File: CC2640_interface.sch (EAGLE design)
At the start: 32 parts, among them Q1 FA-128, Q2 FC-12M

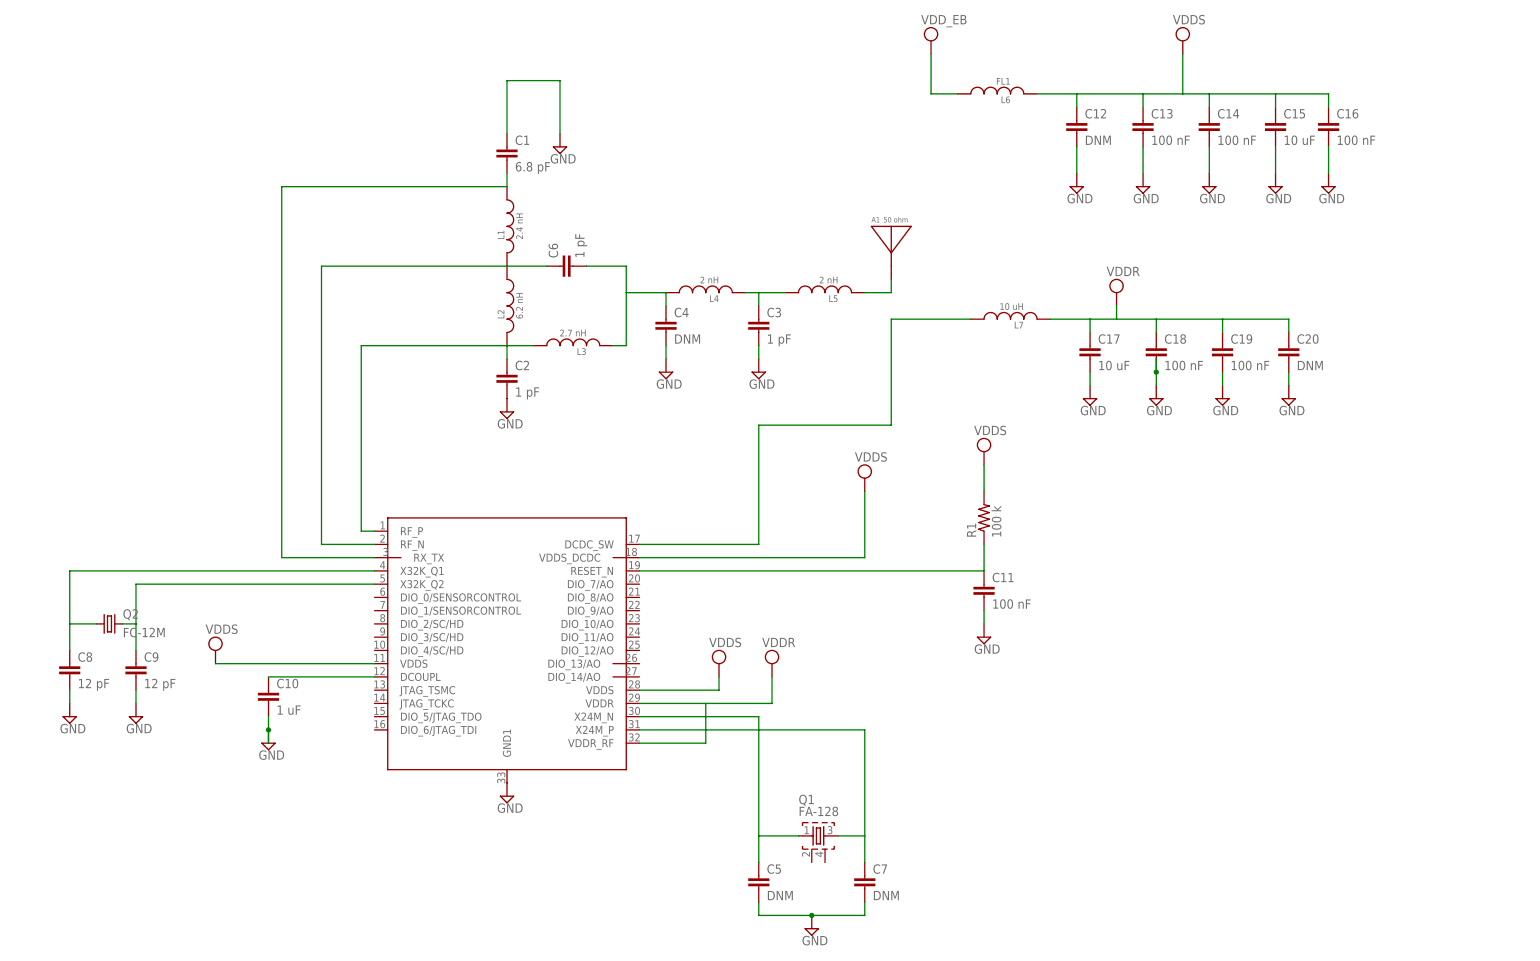
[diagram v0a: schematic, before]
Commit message: cleaned up the schematic
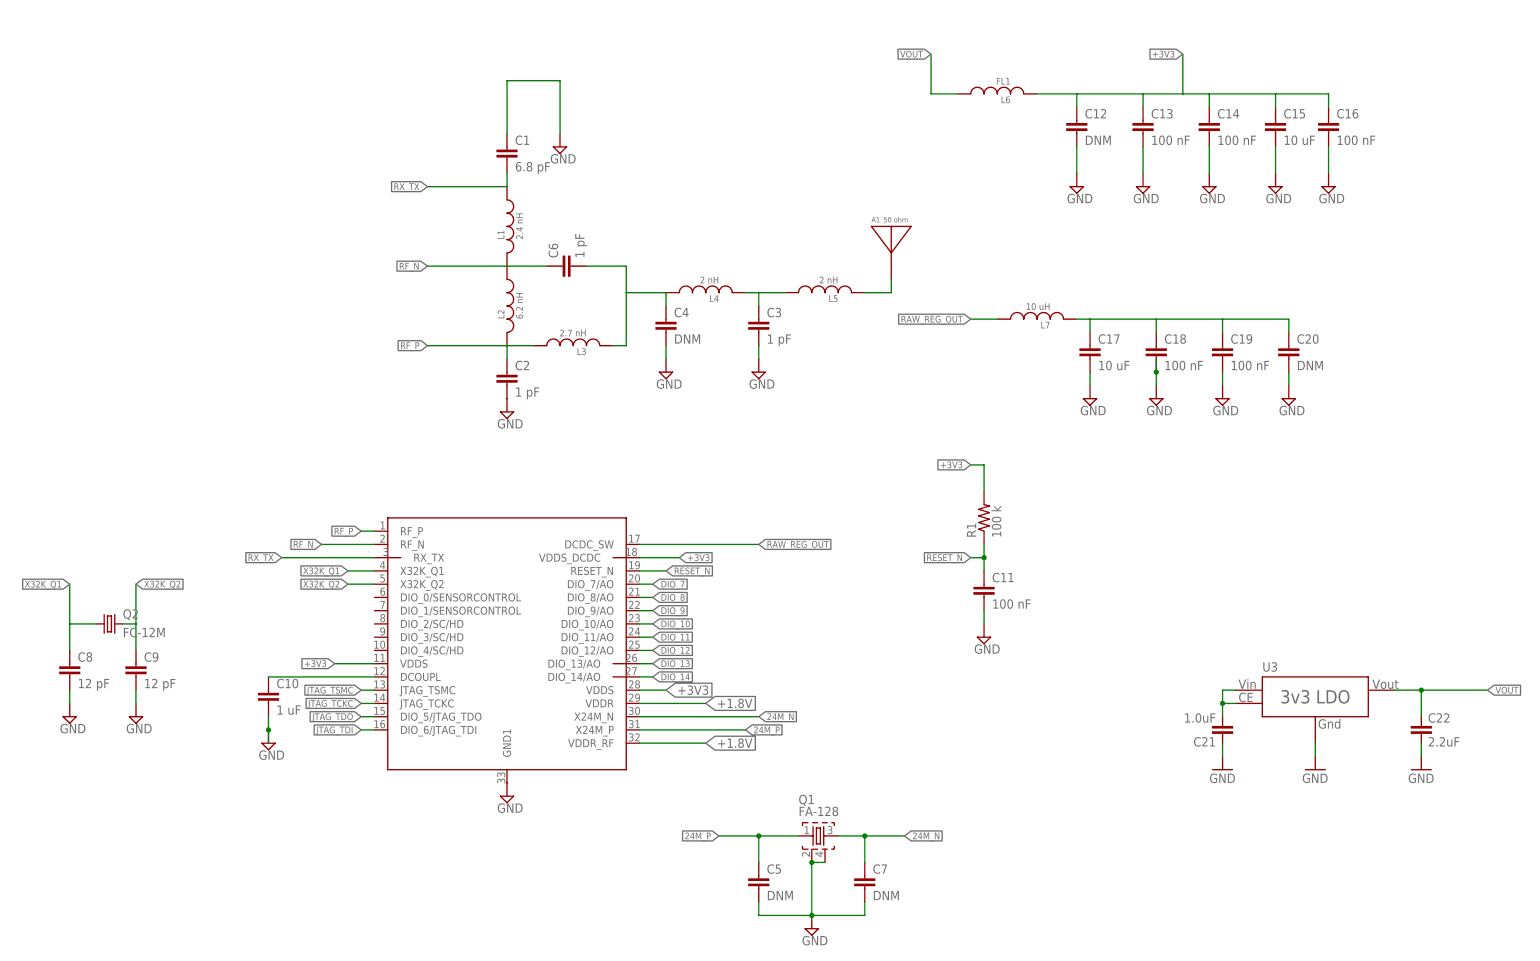
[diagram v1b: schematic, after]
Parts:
- added C21: 1.0uF, Jon_LIB:C-EUC0805
- added C22: 2.2uF, Jon_LIB:C-EUC0805
- added U3: XC6210, MAAV:XC6210
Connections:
- net N$1 renamed RX_TX
- net N$11 renamed DCOUPLE_ME
- net N$14 renamed RAW_REG_OUT
- net N$2 renamed RF_N
- net N$3 renamed RF_P
- net N$6 renamed X32K_Q1
- net N$8 renamed X32K_Q2
- net NRESET renamed RESET_N
- removed net N$10: C7.1, Q1.3, U$1.X24M_P
- removed net N$9: C5.1, Q1.1, U$1.X24M_N
- removed net VDD: C12.1, C13.1, C14.1, C15.1, C16.1, C17.1, C18.1, C19.1, C20.1, L6.1, L6.2, L7.2, R1.2, U$1.VDDR, U$1.VDDR_RF, U$1.VDDS, U$1.VDDS@2, U$1.VDDS_DCDC
- new net +1.8V: C17.1, C18.1, C19.1, C20.1, L7.2, U$1.VDDR, U$1.VDDR_RF
- new net +3V3: C12.1, C13.1, C14.1, C15.1, C16.1, L6.2, R1.2, U$1.VDDS, U$1.VDDS@2, U$1.VDDS_DCDC
- new net 24M_N: C7.1, Q1.3, U$1.X24M_N
- new net 24M_P: C5.1, Q1.1, U$1.X24M_P
- new net DIO_10: U$1.DIO_10/AO
- new net DIO_11: U$1.DIO_11/AO
- new net DIO_12: U$1.DIO_12/AO
- new net DIO_13: U$1.DIO_13/AO
- new net DIO_14: U$1.DIO_14/AO
- new net DIO_7: U$1.DIO_7/AO
- new net DIO_8: U$1.DIO_8/AO
- new net DIO_9: U$1.DIO_9/AO
- new net JTAG_TCKC: U$1.JTAG_TCKC
- new net JTAG_TDI: U$1.DIO_6/JTAG_TDI
- new net JTAG_TDO: U$1.DIO_5/JTAG_TDO
- new net JTAG_TSMC: U$1.JTAG_TSMC
- new net VBATT: C21.2, U3.CE, U3.VIN
- new net VOUT: C22.1, L6.1, U3.VOUT
- net GND: now also C21.1, C22.2, Q1.2, Q1.4, U3.GND
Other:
- moved on the sheet: L7

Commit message: added mpu, cleaned up sch
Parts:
- removed A1: 50 ohm, chips:AH212M
- added ANT: 2450AT18A100, Johanson_antenna:2450AT18A100
- added C23, C24: 0.1uF, SparkFun-Capacitors:0.1UF-25V(+80/-20%)(0603)
- added R4: 10K, SparkFun-Resistors:10KOHM-1/10W-1%(0603)0603
- added SJ1: JUMPER-PAD-2-NC_BY_PASTEFULL-BOX-SILK, SparkFun-Passives:JUMPER-PAD-2-NC_BY_PASTEFULL-BOX-SILK
- added U1: MPU-9250, Testing:MPU-9250
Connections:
- new net ADSD_STUB: U1.AD0/SDO
- new net AUX_CL: U1.AUX_CL
- new net AUX_DA: U1.AUX_DA
- new net DIO_1: R4.1, U$1.DIO_1/SENSORCONTROL, U1.!CS
- new net FSYNC: U1.FSYNC
- new net INT: U1.INT
- new net REGOUT: C23.1, U1.REGOUT
- new net VDDIO: SJ1.2
- net +3V3: now also C24.1, R4.2, SJ1.1, U1.VDD, U1.VDDIO
- net DIO_11: now also U1.SCL/SCLK
- net DIO_12: now also U1.SDA/SDI
- net GND: now also C23.2, C24.2, U1.GND
- net N$7: now also ANT.P$1; no longer A1.ANTENNA
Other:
- note added: "there may need to be more passives here"
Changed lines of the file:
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@@
 <layer number="112" name="tSilk" color="7" fill="1" visible="yes" active="yes"/>
 <layer number="113" name="IDFDebug" color="7" fill="1" visible="yes" active="yes"/>
+<layer number="114" name="Badge_Outline" color="11" fill="1" visible="no" active="no"/>
+<layer number="115" name="ReferenceISLANDS" color="7" fill="1" visible="yes" active="yes"/>
 <layer number="116" name="Patch_BOT" color="9" fill="4" visible="yes" active="yes"/>
 <layer number="118" name="Rect_Pads" color="7" fill="1" visible="yes" active="yes"/>
@@
 <part name="SUPPLY3" library="supply2" deviceset="GND" device=""/>
 <part name="SUPPLY4" library="supply2" deviceset="GND" device=""/>
-<part name="A1" library="chips" deviceset="AH212M" device="" value="50 ohm"/>
 <part name="Q1" library="crystal" deviceset="FA-" device="128"/>
 <part name="Q2" library="crystal" deviceset="FC-12M" device=""/>
@@
 <part name="GND30" library="supply1" deviceset="GND" device=""/>
 <part name="U3" library="MAAV" deviceset="XC6210" device=""/>
+<part name="U1" library="Testing" deviceset="MPU-9250" device=""/>
+<part name="GND2" library="SparkFun-Aesthetics" deviceset="GND" device=""/>
+<part name="SUPPLY10" library="SparkFun-Aesthetics" deviceset="VCC" device="" value="VDD"/>
+<part name="SJ1" library="SparkFun-Passives" deviceset="JUMPER-PAD-2-NC_BY_PASTE" device="FULL-BOX-SILK"/>
+<part name="C23" library="SparkFun-Capacitors" deviceset="0.1UF-25V(+80/-20%)(0603)" device="" value="0.1uF"/>
+<part name="C24" library="SparkFun-Capacitors" deviceset="0.1UF-25V(+80/-20%)(0603)" device="" value="0.1uF"/>
+<part name="GND3" library="SparkFun-Aesthetics" deviceset="GND" device=""/>
+<part name="R4" library="SparkFun-Resistors" deviceset="10KOHM-1/10W-1%(0603)" device="0603" value="10K"/>
+<part name="ANT" library="Johanson_antenna" deviceset="2450AT18A100" device=""/>
 </parts>
 <sheets>
 <sheet>
 <plain>
+<text x="175.26" y="165.1" size="2.1844" layer="91">there may need to be  more passives here</text>
 </plain>
 <instances>
@@
 <instance part="SUPPLY3" gate="GND" x="114.3" y="129.54"/>
 <instance part="SUPPLY4" gate="GND" x="124.46" y="180.34"/>
-<instance part="A1" gate="G$1" x="187.96" y="160.02"/>
 <instance part="Q1" gate="G$1" x="172.72" y="48.26"/>
 <instance part="Q2" gate="G$1" x="38.1" y="88.9"/>
@@
 <instance part="GND30" gate="1" x="289.56" y="60.96"/>
 <instance part="U3" gate="G$1" x="269.24" y="73.66"/>
+<instance part="ANT" gate="G$1" x="187.96" y="160.02"/>
 </instances>
 <busses>
@@
 <segment>
 <pinref part="L5" gate="G$1" pin="2"/>
-<pinref part="A1" gate="G$1" pin="ANTENNA"/>
 <wire x1="182.88" y1="152.4" x2="187.96" y2="152.4" width="0.1524" layer="91"/>
 <wire x1="187.96" y1="152.4" x2="187.96" y2="154.94" width="0.1524" layer="91"/>
+<pinref part="ANT" gate="G$1" pin="P$1"/>
 </segment>
 </net>
@@
 </segment>
 </net>
+<net name="DIO_1" class="0">
+<segment>
+<pinref part="U$1" gate="G$1" pin="DIO_1/SENSORCONTROL"/>
+<wire x1="88.9" y1="91.44" x2="86.36" y2="91.44" width="0.1524" layer="91"/>
+<label x="86.36" y="91.44" size="1.778" layer="95" rot="R180" xref="yes"/>
+</segment>
+</net>
+</nets>
+</sheet>
+<sheet>
+<plain>
+</plain>
+<instances>
+<instance part="U1" gate="G$1" x="100.076" y="103.124"/>
+<instance part="GND2" gate="1" x="77.216" y="82.804"/>
+<instance part="SUPPLY10" gate="G$1" x="64.516" y="118.364"/>
+<instance part="SJ1" gate="G$1" x="46.736" y="141.224" smashed="yes"/>
+<instance part="C23" gate="G$1" x="74.676" y="92.964" rot="MR0"/>
+<instance part="C24" gate="G$1" x="64.516" y="103.124" rot="MR0"/>
+<instance part="GND3" gate="1" x="64.516" y="95.504"/>
+<instance part="R4" gate="G$1" x="148.336" y="113.284" rot="R90"/>
+</instances>
+<busses>
+</busses>
+<nets>
+<net name="GND" class="0">
+<segment>
+<pinref part="U1" gate="G$1" pin="GND"/>
+<pinref part="GND2" gate="1" pin="GND"/>
+<wire x1="82.296" y1="98.044" x2="79.756" y2="98.044" width="0.1524" layer="91"/>
+<wire x1="79.756" y1="98.044" x2="79.756" y2="87.884" width="0.1524" layer="91"/>
+<wire x1="79.756" y1="87.884" x2="77.216" y2="87.884" width="0.1524" layer="91"/>
+<wire x1="77.216" y1="87.884" x2="77.216" y2="85.344" width="0.1524" layer="91"/>
+<pinref part="C23" gate="G$1" pin="2"/>
+<wire x1="74.676" y1="90.424" x2="74.676" y2="87.884" width="0.1524" layer="91"/>
+<wire x1="74.676" y1="87.884" x2="77.216" y2="87.884" width="0.1524" layer="91"/>
+<junction x="77.216" y="87.884"/>
+</segment>
+<segment>
+<pinref part="C24" gate="G$1" pin="2"/>
+<pinref part="GND3" gate="1" pin="GND"/>
+<wire x1="64.516" y1="98.044" x2="64.516" y2="100.584" width="0.1524" layer="91"/>
+</segment>
+</net>
+<net name="VDDIO" class="0">
+<segment>
+<wire x1="54.356" y1="141.224" x2="51.816" y2="141.224" width="0.1524" layer="91"/>
+<pinref part="SJ1" gate="G$1" pin="2"/>
+<label x="54.356" y="141.224" size="1.27" layer="95" xref="yes"/>
+</segment>
+</net>
+<net name="INT" class="0">
+<segment>
+<pinref part="U1" gate="G$1" pin="INT"/>
+<wire x1="82.296" y1="105.664" x2="79.756" y2="105.664" width="0.1524" layer="91"/>
+<label x="79.756" y="105.664" size="1.27" layer="95" rot="R180" xref="yes"/>
+</segment>
+</net>
+<net name="FSYNC" class="0">
+<segment>
+<pinref part="U1" gate="G$1" pin="FSYNC"/>
+<wire x1="82.296" y1="103.124" x2="79.756" y2="103.124" width="0.1524" layer="91"/>
+<label x="79.756" y="103.124" size="1.27" layer="95" rot="R180" xref="yes"/>
+</segment>
+</net>
+<net name="REGOUT" class="0">
+<segment>
+<pinref part="U1" gate="G$1" pin="REGOUT"/>
+<pinref part="C23" gate="G$1" pin="1"/>
+<wire x1="82.296" y1="100.584" x2="74.676" y2="100.584" width="0.1524" layer="91"/>
+<wire x1="74.676" y1="100.584" x2="74.676" y2="98.044" width="0.1524" layer="91"/>
+</segment>
+</net>
+<net name="AUX_CL" class="0">
+<segment>
+<pinref part="U1" gate="G$1" pin="AUX_CL"/>
+<wire x1="117.856" y1="110.744" x2="120.396" y2="110.744" width="0.1524" layer="91"/>
+<label x="120.396" y="110.744" size="1.27" layer="95" xref="yes"/>
+</segment>
+</net>
+<net name="AUX_DA" class="0">
+<segment>
+<pinref part="U1" gate="G$1" pin="AUX_DA"/>
+<wire x1="117.856" y1="108.204" x2="120.396" y2="108.204" width="0.1524" layer="91"/>
+<label x="120.396" y="108.204" size="1.27" layer="95" xref="yes"/>
+</segment>
+</net>
+<net name="DIO_1" class="0">
+<segment>
+<pinref part="U1" gate="G$1" pin="!CS"/>
+<wire x1="117.856" y1="105.664" x2="148.336" y2="105.664" width="0.1524" layer="91"/>
+<label x="150.876" y="105.664" size="1.27" layer="95" xref="yes"/>
+<pinref part="R4" gate="G$1" pin="1"/>
+<wire x1="148.336" y1="105.664" x2="150.876" y2="105.664" width="0.1524" layer="91"/>
+<wire x1="148.336" y1="108.204" x2="148.336" y2="105.664" width="0.1524" layer="91"/>
+<junction x="148.336" y="105.664"/>
+</segment>
+</net>
+<net name="DIO_11" class="0">
+<segment>
+<pinref part="U1" gate="G$1" pin="SCL/SCLK"/>
+<wire x1="117.856" y1="103.124" x2="150.876" y2="103.124" width="0.1524" layer="91"/>
+<label x="150.876" y="103.124" size="1.27" layer="95" xref="yes"/>
+</segment>
+</net>
+<net name="DIO_12" class="0">
+<segment>
+<pinref part="U1" gate="G$1" pin="SDA/SDI"/>
+<label x="150.876" y="100.584" size="1.27" layer="95" xref="yes"/>
+<wire x1="117.856" y1="100.584" x2="150.876" y2="100.584" width="0.1524" layer="91"/>
+</segment>
+</net>
+<net name="DIO_14" class="0">
+<segment>
+<wire x1="122.936" y1="98.044" x2="138.176" y2="98.044" width="0.1524" layer="91"/>
+<label x="138.176" y="98.044" size="1.27" layer="95" xref="yes"/>
+</segment>
+</net>
+<net name="ADSD_STUB" class="0">
+<segment>
+<pinref part="U1" gate="G$1" pin="AD0/SDO"/>
+<wire x1="117.856" y1="98.044" x2="122.936" y2="98.044" width="0.1524" layer="91"/>
+</segment>
+</net>
+<net name="+3V3" class="0">
+<segment>
+<wire x1="39.116" y1="141.224" x2="41.656" y2="141.224" width="0.1524" layer="91"/>
+<pinref part="SJ1" gate="G$1" pin="1"/>
+<label x="39.116" y="141.224" size="1.27" layer="95" rot="R180" xref="yes"/>
+</segment>
+<segment>
+<pinref part="SUPPLY10" gate="G$1" pin="VCC"/>
+<wire x1="64.516" y1="118.364" x2="64.516" y2="110.744" width="0.1524" layer="91"/>
+<pinref part="U1" gate="G$1" pin="VDD"/>
+<wire x1="64.516" y1="110.744" x2="82.296" y2="110.744" width="0.1524" layer="91"/>
+<pinref part="C24" gate="G$1" pin="1"/>
+<wire x1="64.516" y1="110.744" x2="64.516" y2="108.204" width="0.1524" layer="91"/>
+<junction x="64.516" y="110.744"/>
+</segment>
+<segment>
+<label x="130.556" y="120.904" size="1.27" layer="95" font="vector" rot="R180" xref="yes"/>
+<pinref part="R4" gate="G$1" pin="2"/>
+<wire x1="130.556" y1="120.904" x2="148.336" y2="120.904" width="0.1524" layer="91"/>
+<wire x1="148.336" y1="120.904" x2="148.336" y2="118.364" width="0.1524" layer="91"/>
+</segment>
+<segment>
+<pinref part="U1" gate="G$1" pin="VDDIO"/>
+<wire x1="82.296" y1="108.204" x2="79.756" y2="108.204" width="0.1524" layer="91"/>
+<label x="79.756" y="108.204" size="1.27" layer="95" rot="R180" xref="yes"/>
+</segment>
+</net>

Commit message: updated sch and brd
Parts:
- removed C1: 6.8 pF, rcl:C-EUC0402
- removed C21: 1.0uF, Jon_LIB:C-EUC0805
- removed C22: 2.2uF, Jon_LIB:C-EUC0805
- removed C6: 1 pF, rcl:C-EUC0402
- removed L1: 2.4 nH, passives:INDUCTOR0603
- removed L2: 6.2 nH, passives:INDUCTOR0603
- removed U3: XC6210, MAAV:XC6210
- added C25, C26, C29, C39, C40, C41, C43, C44, C45: 100nF/X7R/10%, rcl:C-EUC0603_DWS
- added C27, C32, C34, C35, C48: 10nF/X7R/10%, rcl:C-EUC0603_DWS
- added C28, C37, C38, C42, C46, C49: 1uF/X5R/10%, rcl:C-EUC0603_DWS
- added C30, C31: 100pF/COG/5%, rcl:C-EUC0603_DWS
- added C33, C36: 1nF/X7R/10%, rcl:C-EUC0603_DWS
- added C47: 47µF/10%/6.3V/TANT(C)/ESR/0.25ohm(TR3C476K6R3C0250/1754044), rcl:CPOL-EUCT6032
- added C50, C51: NA, rcl:C-EUC0603_DWS_NA
- added C52, C53: 10µF/6.3V/0805, rcl:C-EUC0805_5MIL_DWS
- added C54, C55: 4.7uF, SparkFun:CAP0402-CAP
- added C56: 1.0uF, Jon_LIB:C-EUC0805
- added C57: 2.2uF, Jon_LIB:C-EUC0805
- added D1, D2: BAV199(1156415), semicon-smd-ipc:DIODE_AC-AC_
- added D4: Red_Led, SparkFun:LED0603
- added DIG_POT: MCP41HVX1, chips:MCP41HVX1
- added IC1: MCP607-I/SN, linear:LM358D
- added IC2: TLC277IDR, linear:LM358D
- added L8: 22µH/±10%/1.7ohm/80mA(LB2012T220K/8030984), rcl:L-USL0805_5MIL_DWS
- added PGS1, PGS2: PGB1010603MR(F2594TR-ND), OLIMEX_DISCRET:PGB1010603MR(F2594TR-ND)
- added PWR: GYX-SD-TC0805SURK(RED), DOUBLE-SIDE:LED0805DWS
- added R10, R13: 1M/1%, rcl:R-EU_R0603_5MIL_DWS
- added R11: 1k/1%, rcl:R-EU_R0603_5MIL_DWS
- added R12, R9: 100k/1%, rcl:R-EU_R0603_5MIL_DWS
- added R14: 56k/1%, rcl:R-EU_R0603_5MIL_DWS
- added R15: 330k/1%, rcl:R-EU_R0603_5MIL_DWS
- added R16, R18: 3.9k/1%, rcl:R-EU_R0603_5MIL_DWS
- added R17, R21, R22, R23, R30, R31: 10k/1%, rcl:R-EU_R0603_5MIL_DWS
- added R19: 470, SparkFun:RESISTOR0402-RES
- added R2, R20, R29, R3, R34, R5, R6: 2k/1%, rcl:R-EU_R0603_5MIL_DWS
- added R24: 12.5k, SparkFun:RESISTOR0402-RES
- added R32, R33: 0R(boad mounted), OLIMEX_DISCRET:R_0R0R(NA)
- added R7, R8: NA(3.3M), rcl:R-EU_R0603_5MIL_DWS_NA
- added SR1: AP431SA, OLIMEX_IC:TL431'''
- added SV1: (no value), con-lstb:MA03-1
- added U2: INA321EA, OLIMEX_IC:INA321EA
- added U4: MCP73831, SparkFun:MCP73831
- added U6: XC6210, MAAV:XC6210
- added X1: USB-MICROB, SparkFun:USB-MICROB
- added Z1: BZV55C6V2, gogo:ZDIOD-SMD
- C2: value 1 pF -> 1.2 pF
- C4: value DNM -> 1.2pF
- L3: value 2.7 nH -> 2 nH
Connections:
- net 24M_N renamed 24M_NEGA
- new net 5VIN: C54.1, D4.A, U4.VIN, X1.VBUS
- new net ADC0: C28.1, R18.1
- new net CH1_IN+: PGS2.1, R2.1, SV1.1
- new net CH1_IN-: PGS1.2, R3.1, SV1.3
- new net DIO_2: DIG_POT.CS_AL, U$1.DIO_2/SC/HD
- new net GNDA: C25.2, C26.2, C27.2, C28.2, C29.2, C40.1, C41.2, C44.2, C45.2, C46.2, C47.-, C48.2, C49.2, C52.2, C53.2, IC1P.V-, IC2P.V-, R21.1, R23.1, R29.1, SR1.A, U2.V-, Z1.A
- new net N$1: D1.AK, R3.2, R5.2, R7.2
- new net N$10: R30.1, R31.2, U2.RG
- new net N$102: C51.1, IC1A.+IN, R33.1.2
- new net N$104: C33.2, C37.1, C50.2, IC1A.OUT, R12.2
- new net N$105: C33.1, IC1A.-IN, R11.1, R12.1
- new net N$107: C35.1, IC1B.+IN, R15.2
- new net N$108: C34.1, R14.2, R15.1
- new net N$109: C34.2, C36.2, IC1B.OUT, R17.2, R18.2
- new net N$11: L8.1, PWR.A
- new net N$110: C36.1, IC1B.-IN, R16.1, R17.1
- new net N$12: DIG_POT.SHDWN_AL
- new net N$14: R19.1, U4.STAT
- new net N$145: C42.1, IC2B.-IN, R9.1
- new net N$15: PWR.C, R29.2
- new net N$2: R24.1, U4.PROG
- new net N$22: R20.1, R21.2, SR1.R
- new net N$3: D4.C, R19.2
- new net N$37: C38.2, R10.1, R32.1.1
- new net N$38: C50.1, R32.1.2, R33.1.1
- new net N$39: PGS1.1, PGS2.2, R34.1, SV1.2
- new net N$6: DIG_POT.WLAT_EN_AL
- new net N$8: D2.AK, R2.2, R6.2, R8.2
- new net N$81: C37.2, R13.1, R14.1
- new net N$83: C38.1, R31.1, R9.2, U2.VOUT
- new net N$9: C42.2, IC2B.OUT, R30.2, U2.REF
- new net N$92: C30.1, C32.1, R6.1, U2.VIN+
- new net N$93: C31.2, C32.2, R5.1, U2.VIN-
- new net POT_A: DIG_POT.POT_A, R11.2
- new net VCC/2: C30.2, C31.1, C35.2, C39.2, C40.2, C43.1, C44.1, C47.+, C51.2, D1.A, D2.A, DIG_POT.POT_B, DIG_POT.POT_W, IC2A.-IN, IC2A.OUT, IC2B.+IN, R10.2, R13.2, R16.2, R34.2, R7.1, R8.1
- new net VCC/2_UNBUFF: C48.1, IC2A.+IN, R22.1, R23.2
- net +3V3: now also C25.1, C26.1, C27.1, C29.1, C39.1, C41.1, C43.2, C45.1, C46.1, C49.1, C52.1, C53.1, D1.K, D2.K, DIG_POT.ANALOG_POS, DIG_POT.VDD, IC1P.V+, IC2P.V+, L8.2, R20.2, R22.2, SR1.C, U2.SHUTDOWN, U2.V+, Z1.C
- net DIO_11: now also DIG_POT.SCK
- net DIO_12: now also DIG_POT.SDI
- net DIO_14: now also DIG_POT.SDO
- net GND: now also C54.2, C55.2, C56.1, C57.2, DIG_POT.ANALOG_NEG, DIG_POT.GND, R24.2, U4.VSS, U6.GND, X1.GND; no longer C1.1, C21.1, C22.2, Q1.2, Q1.4, U3.GND
- net N$4: no longer C6.2
- net RF_N: no longer C6.1, L1.2, L2.1
- net RF_P: no longer L2.2
- net RX_TX: no longer C1.2, L1.1
- net VBATT: now also C55.1, C56.2, U4.VBAT, U6.CE, U6.VIN; no longer C21.2, U3.CE, U3.VIN
- net VOUT: now also C57.1, U6.VOUT; no longer C22.1, U3.VOUT
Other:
- note added: "1 pole"
- note added: "1.5V_REF_BUF"
- note added: "3rd order "Besselworth" filter, fc = 40Hz."
- note added: "Fc=0.16Hz"
- note added: "G= (R17/R16)+1= 3.56"
- note added: "G=1+R12/(TR1+R11)"
- note added: "G=5*(1+R8/R7)=10"
- note added: "G=5,76...101"
- note added: "HF rejection"
- note added: "High Voltage protection"
- note added: "High-Pass filter"
- note added: "Instrumental Amplifier"
- note added: "OAmp with regulated gain!"
- note added: "the digital pot connects vcc/2 to pot_a"
